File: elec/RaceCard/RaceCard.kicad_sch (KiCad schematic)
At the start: 0 parts

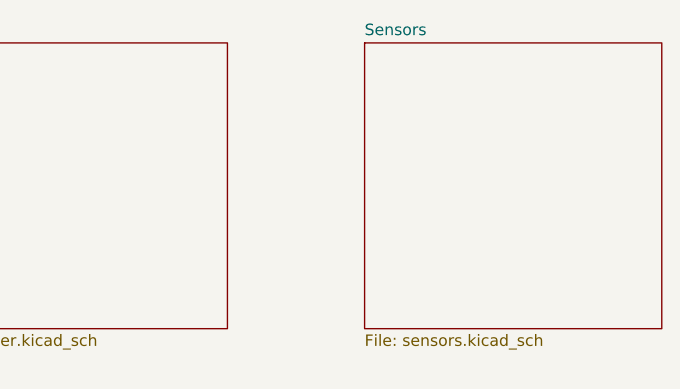
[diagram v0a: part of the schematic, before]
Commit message: schematic slider + btns (à valider)
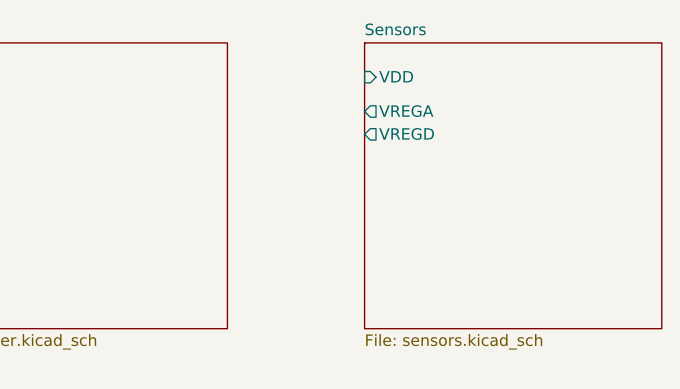
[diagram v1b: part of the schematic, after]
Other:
- sheet Sensors ports: added VDD, VREGA, VREGD; removed none
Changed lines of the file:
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@@
+			)
+		)
+		(pin "VDD" input
+			(at 205.74 67.31 180)
+			(effects
+				(font
+					(size 1.27 1.27)
+				)
+				(justify left)
+			)
+		)
+		(pin "VREGA" output
+			(at 205.74 71.12 180)
+			(effects
+				(font
+					(size 1.27 1.27)
+				)
+				(justify left)
+			)
+		)
+		(pin "VREGD" output
+			(at 205.74 73.66 180)
+			(effects
+				(font
+					(size 1.27 1.27)
+				)
+				(justify left)
 			)
 		)

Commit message: Choses manquantes
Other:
- note added: "METTRE LES CONNEXION ENTRE LES PAGES"
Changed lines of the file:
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@@
 		(rev "Rev.1")
+	)
+	(text "METTRE LES CONNEXION ENTRE LES PAGES"
+		(exclude_from_sim no)
+		(at 146.05 51.308 0)
+		(effects
+			(font
+				(size 2.54 2.54)
+				(thickness 0.254)
+				(bold yes)
+				(color 255 0 0 1)
+			)
+		)
 	)
 	(sheet

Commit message: Commence plugger choses
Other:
- sheet Power ports: added VDD; removed none
- sheet RF ports: added VDD; removed none
- sheet STM32 ports: added VDD; removed none
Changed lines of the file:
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@@
 		)
 	)
-	(sheet
-		(at 157.48 107.95)
-		(size 33.02 19.685)
+	(junction
+		(at 52.07 114.3)
+		(diameter 0)
+		(color 0 0 0 0)
+	)
+	(junction
+		(at 52.07 64.77)
+		(diameter 0)
+		(color 0 0 0 0)
+	)
+	(wire
+		(pts
+			(xy 52.07 64.77) (xy 52.07 114.3)
+		)
+		(stroke
+			(width 0)
+			(type default)
+		)
+	)
+	(wire
+		(pts
+			(xy 77.47 153.67) (xy 52.07 153.67)
+		)
+		(stroke
+			(width 0)
+			(type default)
+		)
+	)
+	(wire
+		(pts
+			(xy 52.07 64.77) (xy 77.47 64.77)
+		)
+		(stroke
+			(width 0)
+			(type default)
+		)
+	)
+	(wire
+		(pts
+			(xy 77.47 114.3) (xy 52.07 114.3)
+		)
+		(stroke
+			(width 0)
+			(type default)
+		)
+	)
+	(wire
+		(pts
+			(xy 52.07 64.77) (xy 49.53 64.77)
+		)
+		(stroke
+			(width 0)
+			(type default)
+		)
+	)
+	(wire
+		(pts
+			(xy 52.07 153.67) (xy 52.07 114.3)
+		)
+		(stroke
+			(width 0)
+			(type default)
+		)
+	)
+	(sheet
+		(at 77.47 149.86)
+		(size 33.02 31.75)
 		(exclude_from_sim no)
 		(in_bom yes)
@@
 		)
 		(property "Sheetname" "RF"
-			(at 157.48 107.2384 0)
+			(at 77.47 149.1484 0)
 			(effects
 				(font
@@
 		)
 		(property "Sheetfile" "rf.kicad_sch"
-			(at 157.48 128.2196 0)
-			(effects
-				(font
-					(size 1.27 1.27)
-				)
-				(justify left top)
+			(at 77.47 182.1946 0)
+			(effects
+				(font
+					(size 1.27 1.27)
+				)
+				(justify left top)
+			)
+		)
+		(pin "VDD" input
+			(at 77.47 153.67 180)
+			(effects
+				(font
+					(size 1.27 1.27)
+				)
+				(justify left)
 			)
 		)
@@
 	)
 	(sheet
-		(at 62.865 63.5)
-		(size 64.135 63.5)
+		(at 77.47 55.88)
+		(size 53.34 48.26)
 		(exclude_from_sim no)
 		(in_bom yes)
@@
 		)
 		(property "Sheetname" "STM32"
-			(at 62.865 62.7884 0)
+			(at 77.47 55.1684 0)
 			(effects
 				(font
@@
 		)
 		(property "Sheetfile" "stm32.kicad_sch"
-			(at 62.865 127.5846 0)
-			(effects
-				(font
-					(size 1.27 1.27)
-				)
-				(justify left top)
+			(at 77.47 104.7246 0)
+			(effects
+				(font
+					(size 1.27 1.27)
+				)
+				(justify left top)
+			)
+		)
+		(pin "VDD" input
+			(at 77.47 64.77 180)
+			(effects
+				(font
+					(size 1.27 1.27)
+				)
+				(justify left)
 			)
 		)
@@
 	)
 	(sheet
-		(at 157.48 63.5)
+		(at 16.51 62.23)
 		(size 33.02 31.75)
 		(exclude_from_sim no)
@@
 		)
 		(property "Sheetname" "Power"
-			(at 157.48 62.7884 0)
+			(at 16.51 61.5184 0)
 			(effects
 				(font
@@
 		)
 		(property "Sheetfile" "power.kicad_sch"
-			(at 157.48 95.8346 0)
-			(effects
-				(font
-					(size 1.27 1.27)
-				)
-				(justify left top)
+			(at 16.51 94.5646 0)
+			(effects
+				(font
+					(size 1.27 1.27)
+				)
+				(justify left top)
+			)
+		)
+		(pin "VDD" output
+			(at 49.53 64.77 0)
+			(effects
+				(font
+					(size 1.27 1.27)
+				)
+				(justify right)
 			)
 		)
@@
 	)
 	(sheet
-		(at 205.74 63.5)
+		(at 77.47 110.49)
 		(size 33.02 31.75)
 		(exclude_from_sim no)
@@
 		)
 		(property "Sheetname" "Sensors"
-			(at 205.74 62.7884 0)
+			(at 77.47 109.7784 0)
 			(effects
 				(font
@@
 		)
 		(property "Sheetfile" "sensors.kicad_sch"
-			(at 205.74 95.8346 0)
+			(at 77.47 142.8246 0)
 			(effects
 				(font
@@
 		)
 		(pin "VDD" input
-			(at 205.74 67.31 180)
+			(at 77.47 114.3 180)
 			(effects
 				(font
@@
 		)
 		(pin "VREGA" output
-			(at 205.74 71.12 180)
+			(at 77.47 118.11 180)
 			(effects
 				(font
@@
 		)
 		(pin "VREGD" output
-			(at 205.74 73.66 180)
-			(effects
-				(font
+			(at 77.47 120.65 180)
+			(effects
+				(font

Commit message: Modif
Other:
- sheet RF ports: added DATA; removed none
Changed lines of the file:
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@@
+			)
+		)
+		(pin "DATA" input
+			(at 77.47 157.48 180)
+			(effects
+				(font
+					(size 1.27 1.27)
+				)
+				(justify left)
 			)
 		)

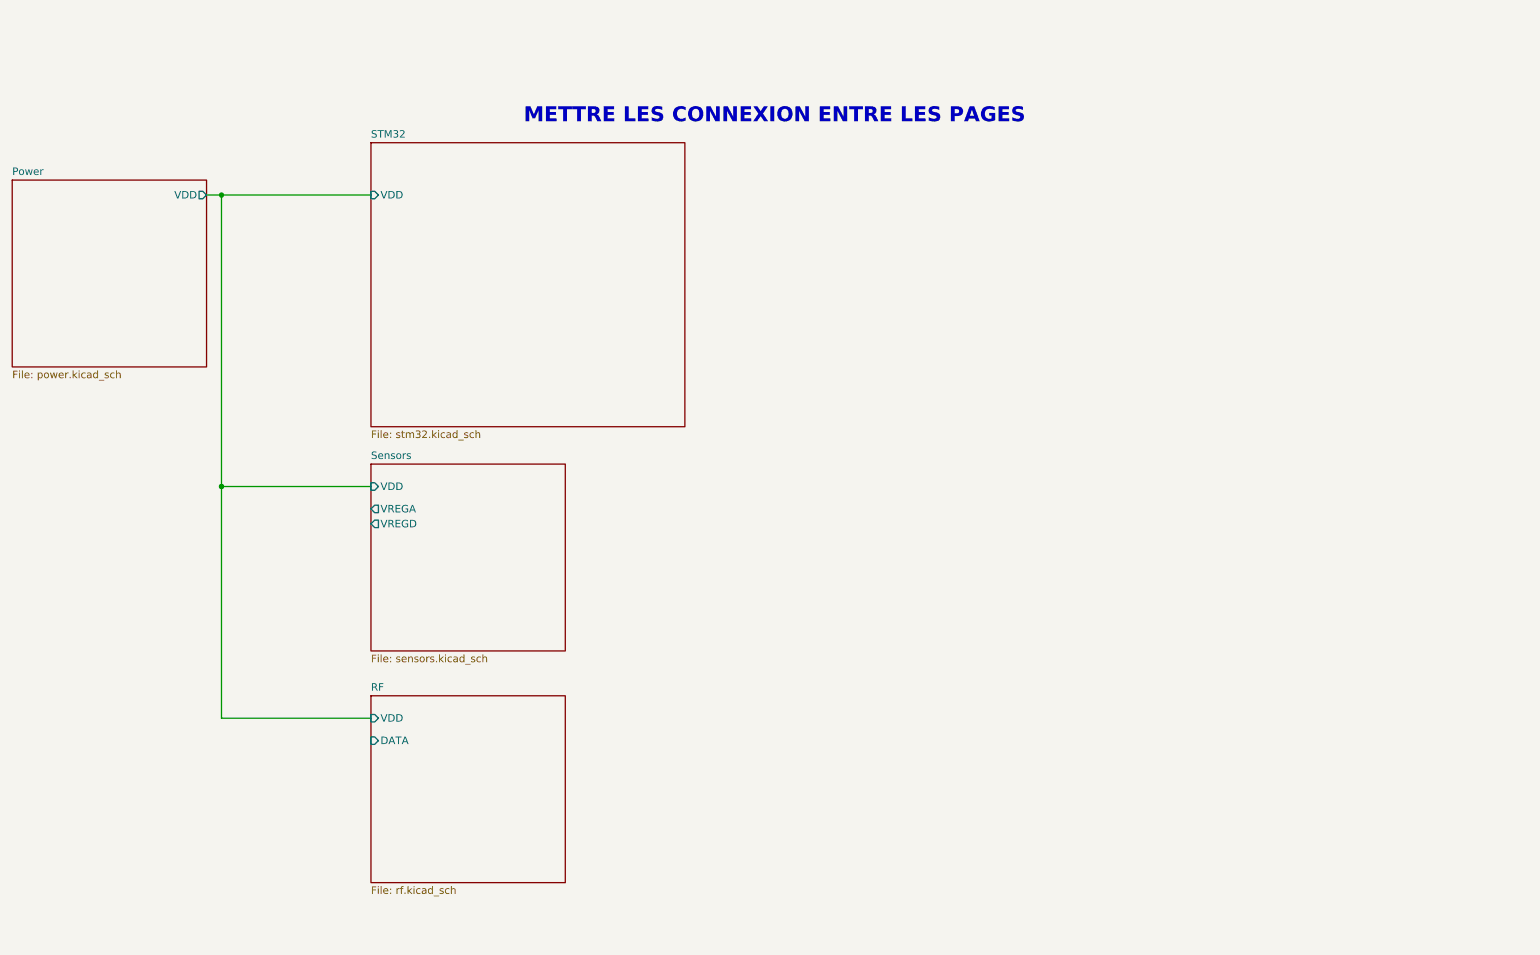
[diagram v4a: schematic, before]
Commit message: ajout connecteur usb c et leds
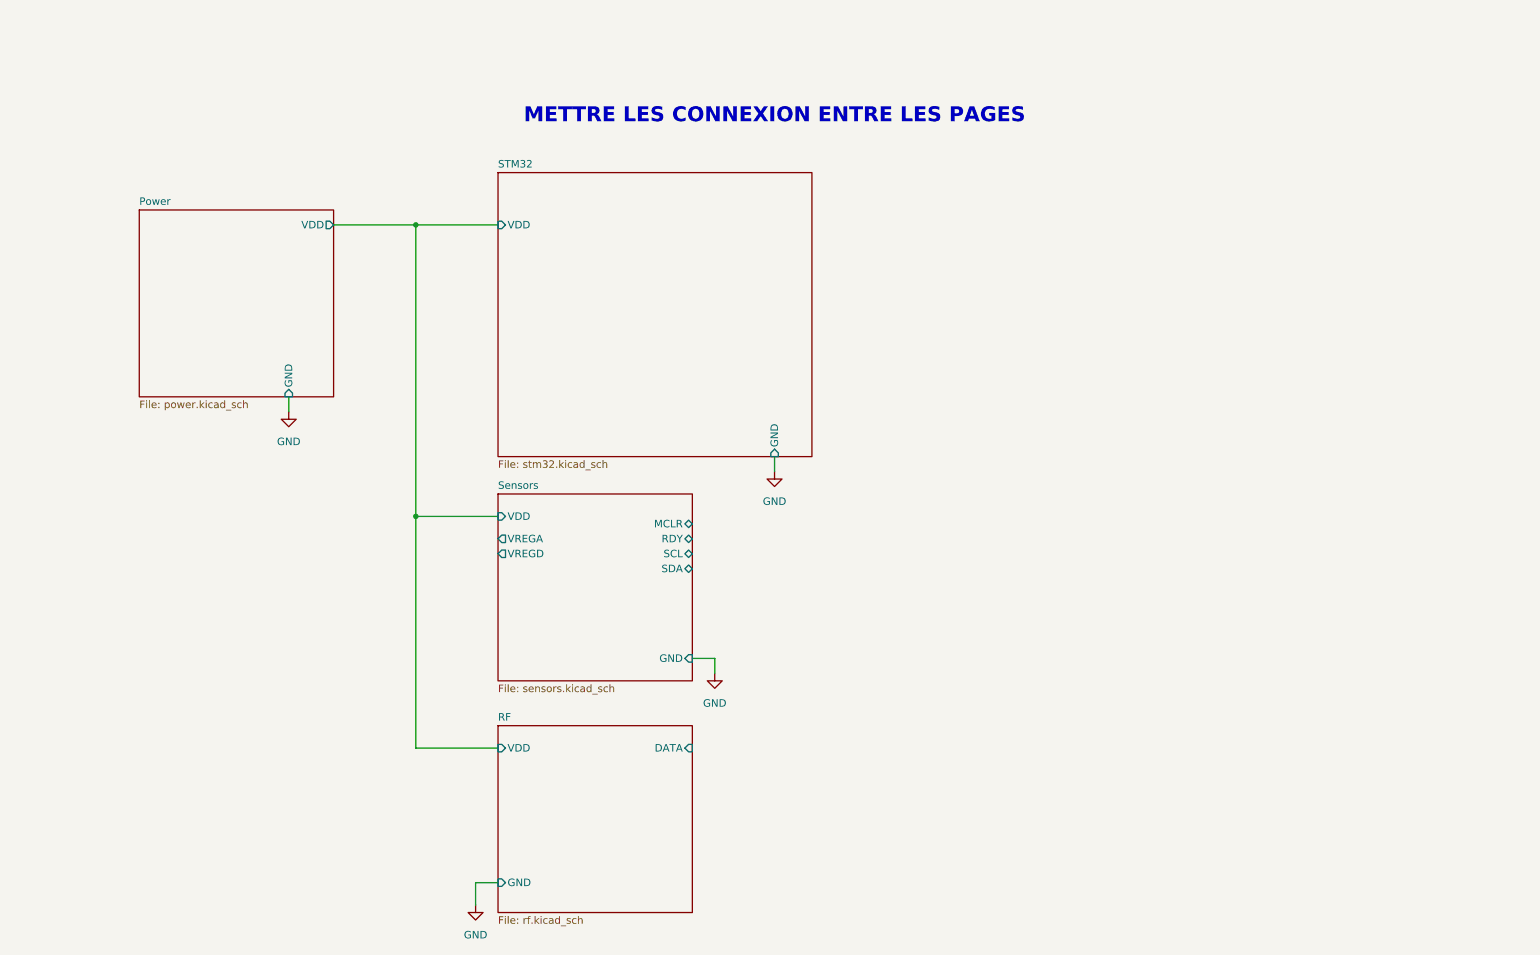
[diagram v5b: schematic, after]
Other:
- sheet Power ports: added GND; removed none
- sheet RF ports: added GND; removed none
- sheet STM32 ports: added GND; removed none
- sheet Sensors ports: added GND, MCLR, RDY, SCL, SDA; removed none

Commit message: + connections stm et autres
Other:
- sheet STM32 ports: added PA1/DATA, PA6/MCLR, PA7/RDY, PB8/I2C1_SCL, PB9/I2C1_SDA; removed none
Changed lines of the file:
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@@
+	(wire
+		(pts
+			(xy 152.4 96.52) (xy 156.21 96.52)
+		)
+		(stroke
+			(width 0)
+			(type default)
+		)
+	)
+	(wire
+		(pts
+			(xy 166.37 69.85) (xy 166.37 158.75)
+		)
+		(stroke
+			(width 0)
+			(type default)
+		)
+	)
+	(wire
+		(pts
+			(xy 152.4 88.9) (xy 163.83 88.9)
+		)
+		(stroke
+			(width 0)
+			(type default)
+		)
+	)
+	(wire
+		(pts
+			(xy 156.21 120.65) (xy 132.08 120.65)
+		)
+		(stroke
+			(width 0)
+			(type default)
+		)
+	)
+	(wire
+		(pts
+			(xy 158.75 123.19) (xy 132.08 123.19)
+		)
+		(stroke
+			(width 0)
+			(type default)
+		)
+	)
+	(wire
+		(pts
+			(xy 156.21 96.52) (xy 156.21 120.65)
+		)
+		(stroke
+			(width 0)
+			(type default)
+		)
+	)
+	(wire
+		(pts
+			(xy 161.29 91.44) (xy 161.29 125.73)
+		)
+		(stroke
+			(width 0)
+			(type default)
+		)
+	)
 	(wire
 		(pts
@@
 	(wire
 		(pts
+			(xy 161.29 125.73) (xy 132.08 125.73)
+		)
+		(stroke
+			(width 0)
+			(type default)
+		)
+	)
+	(wire
+		(pts
 			(xy 99.06 181.61) (xy 95.25 181.61)
 		)
@@
 	(wire
 		(pts
+			(xy 163.83 88.9) (xy 163.83 128.27)
+		)
+		(stroke
+			(width 0)
+			(type default)
+		)
+	)
+	(wire
+		(pts
 			(xy 63.5 99.06) (xy 63.5 101.6)
 		)
@@
 	(wire
 		(pts
+			(xy 152.4 93.98) (xy 158.75 93.98)
+		)
+		(stroke
+			(width 0)
+			(type default)
+		)
+	)
+	(wire
+		(pts
+			(xy 163.83 128.27) (xy 132.08 128.27)
+		)
+		(stroke
+			(width 0)
+			(type default)
+		)
+	)
+	(wire
+		(pts
+			(xy 152.4 69.85) (xy 166.37 69.85)
+		)
+		(stroke
+			(width 0)
+			(type default)
+		)
+	)
+	(wire
+		(pts
+			(xy 158.75 93.98) (xy 158.75 123.19)
+		)
+		(stroke
+			(width 0)
+			(type default)
+		)
+	)
+	(wire
+		(pts
 			(xy 95.25 181.61) (xy 95.25 185.42)
+		)
+		(stroke
+			(width 0)
+			(type default)
+		)
+	)
+	(wire
+		(pts
+			(xy 166.37 158.75) (xy 132.08 158.75)
+		)
+		(stroke
+			(width 0)
+			(type default)
+		)
+	)
+	(wire
+		(pts
+			(xy 152.4 91.44) (xy 161.29 91.44)
 		)
 		(stroke
@@
 			)
 		)
+		(pin "PA1{slash}DATA" input
+			(at 152.4 69.85 0)
+			(effects
+				(font
+					(size 1.27 1.27)
+				)
+				(justify right)
+			)
+		)
+		(pin "PA6{slash}MCLR" input
+			(at 152.4 96.52 0)
+			(effects
+				(font
+					(size 1.27 1.27)
+				)
+				(justify right)
+			)
+		)
+		(pin "PA7{slash}RDY" input
+			(at 152.4 93.98 0)
+			(effects
+				(font
+					(size 1.27 1.27)
+				)
+				(justify right)
+			)
+		)
+		(pin "PB8{slash}I2C1_SCL" bidirectional
+			(at 152.4 91.44 0)
+			(effects
+				(font
+					(size 1.27 1.27)
+				)
+				(justify right)
+			)
+		)
+		(pin "PB9{slash}I2C1_SDA" bidirectional
+			(at 152.4 88.9 0)
+			(effects
+				(font
+					(size 1.27 1.27)
+				)
+				(justify right)
+			)
+		)

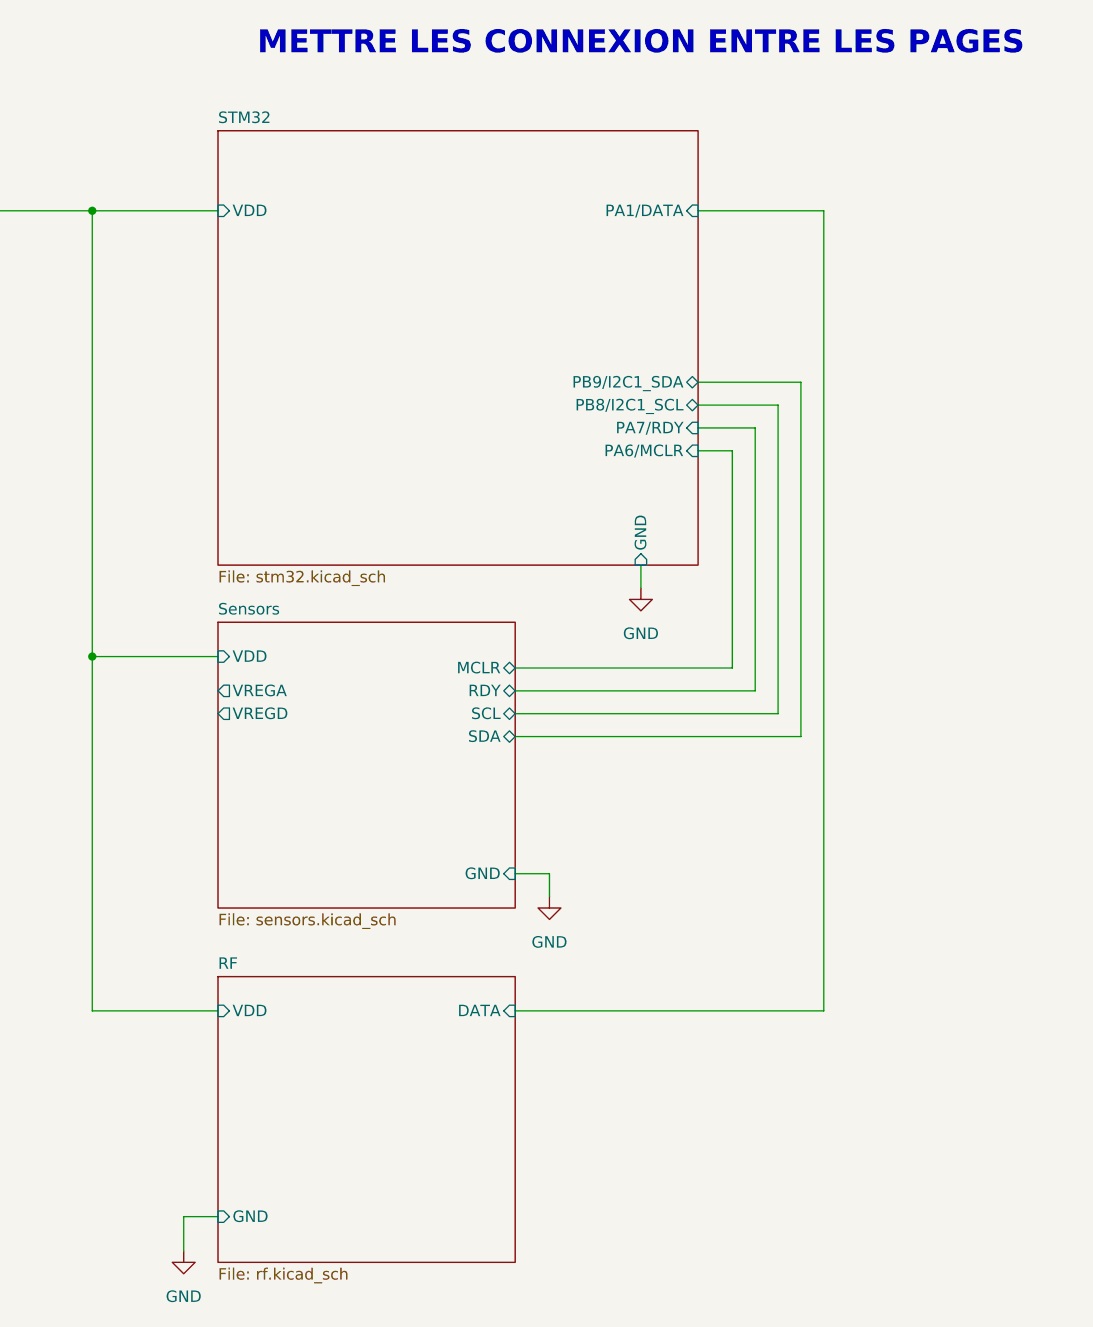
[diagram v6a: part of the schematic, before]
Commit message: + test points
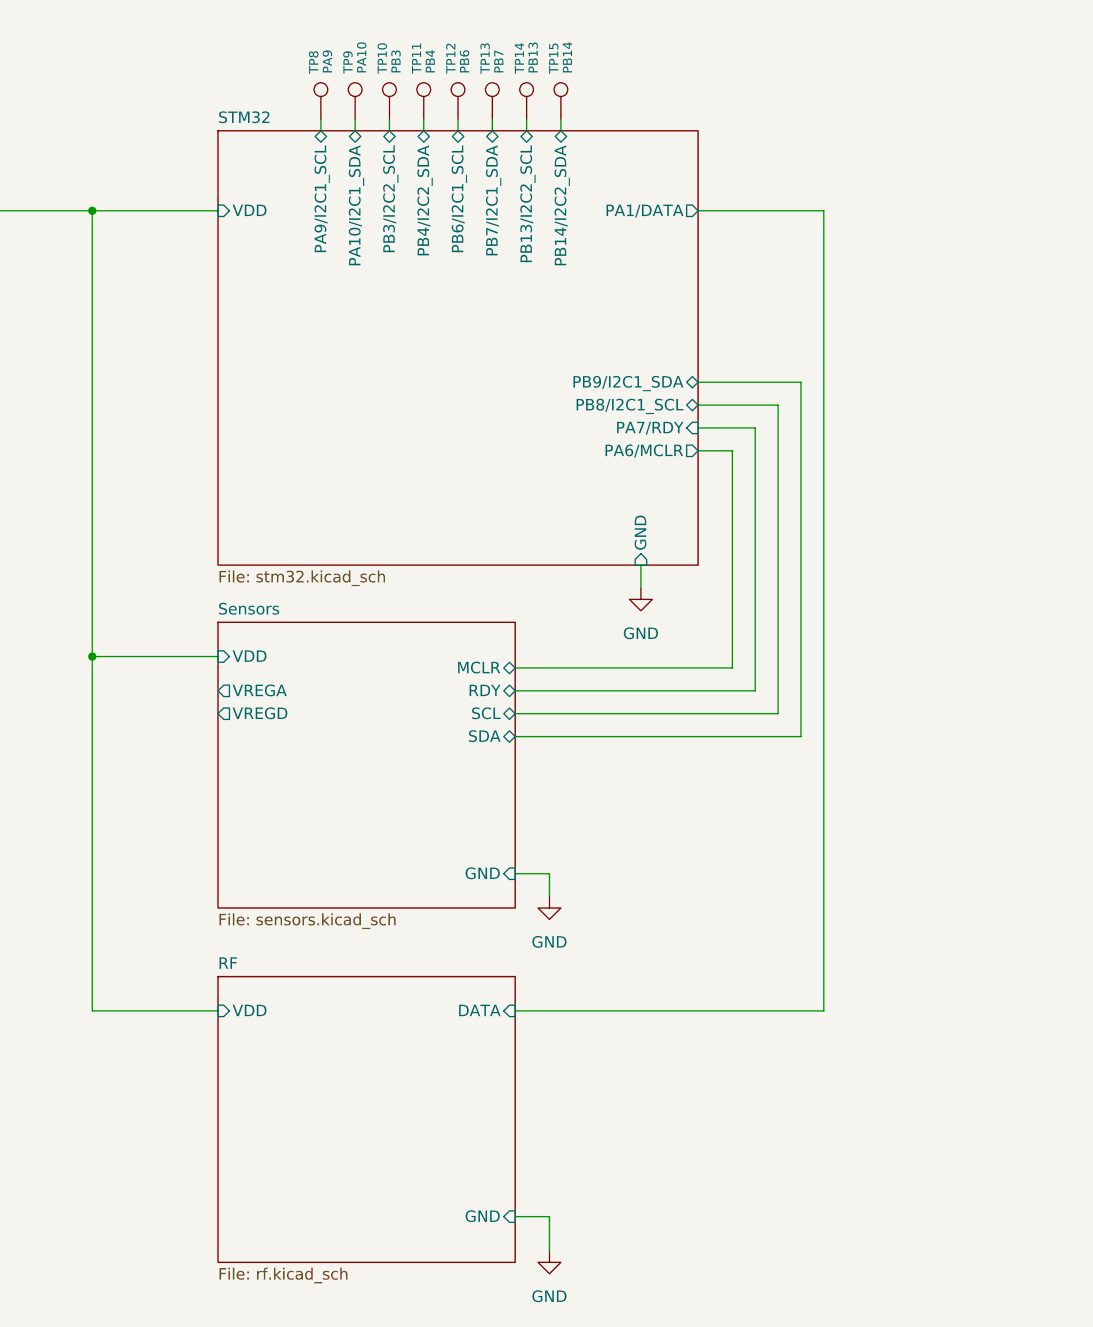
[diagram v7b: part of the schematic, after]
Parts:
- added TP10: PB3, TestPoint:TestPoint_Pad_2.0x2.0mm, symbol Connector:TestPoint
- added TP11: PB4, TestPoint:TestPoint_Pad_2.0x2.0mm, symbol Connector:TestPoint
- added TP12: PB6, TestPoint:TestPoint_Pad_2.0x2.0mm, symbol Connector:TestPoint
- added TP13: PB7, TestPoint:TestPoint_Pad_2.0x2.0mm, symbol Connector:TestPoint
- added TP14: PB13, TestPoint:TestPoint_Pad_2.0x2.0mm, symbol Connector:TestPoint
- added TP15: PB14, TestPoint:TestPoint_Pad_2.0x2.0mm, symbol Connector:TestPoint
- added TP8: PA9, TestPoint:TestPoint_Pad_2.0x2.0mm, symbol Connector:TestPoint
- added TP9: PA10, TestPoint:TestPoint_Pad_2.0x2.0mm, symbol Connector:TestPoint
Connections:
- new net STM32/PA10/I2C1_SDA: TP9.1
- new net STM32/PA9/I2C1_SCL: TP8.1
- new net STM32/PB13/I2C2_SCL: TP14.1
- new net STM32/PB14/I2C2_SDA: TP15.1
- new net STM32/PB3/I2C2_SCL: TP10.1
- new net STM32/PB4/I2C2_SDA: TP11.1
- new net STM32/PB6/I2C1_SCL: TP12.1
- new net STM32/PB7/I2C1_SDA: TP13.1
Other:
- sheet STM32 ports: added PA10/I2C1_SDA, PA9/I2C1_SCL, PB13/I2C2_SCL, PB14/I2C2_SDA, PB3/I2C2_SCL, PB4/I2C2_SDA, PB6/I2C1_SCL, PB7/I2C1_SDA; removed none
- note removed: "METTRE LES CONNEXION ENTRE LES PAGES"

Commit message: petite surprise
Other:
- note added: "RaceCard est un projet qui vise à faire un PCB du format d'une carte de crédit à des fins de contrôle d'une petite voiture téléguidée. Ce projet réalisé par 3 étudiants de génie électrique 69 à l'UdeS a été fait dans le cadre de la compétition C3I H25."
- moved on the sheet: TP10, TP11, TP12, TP13, TP14, TP15, TP8, TP9
